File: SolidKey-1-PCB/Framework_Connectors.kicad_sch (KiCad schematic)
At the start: 2 parts, among them J701 Conn_02x25_Counter_Clockwise, J702 Conn_02x25_Counter_Clockwise

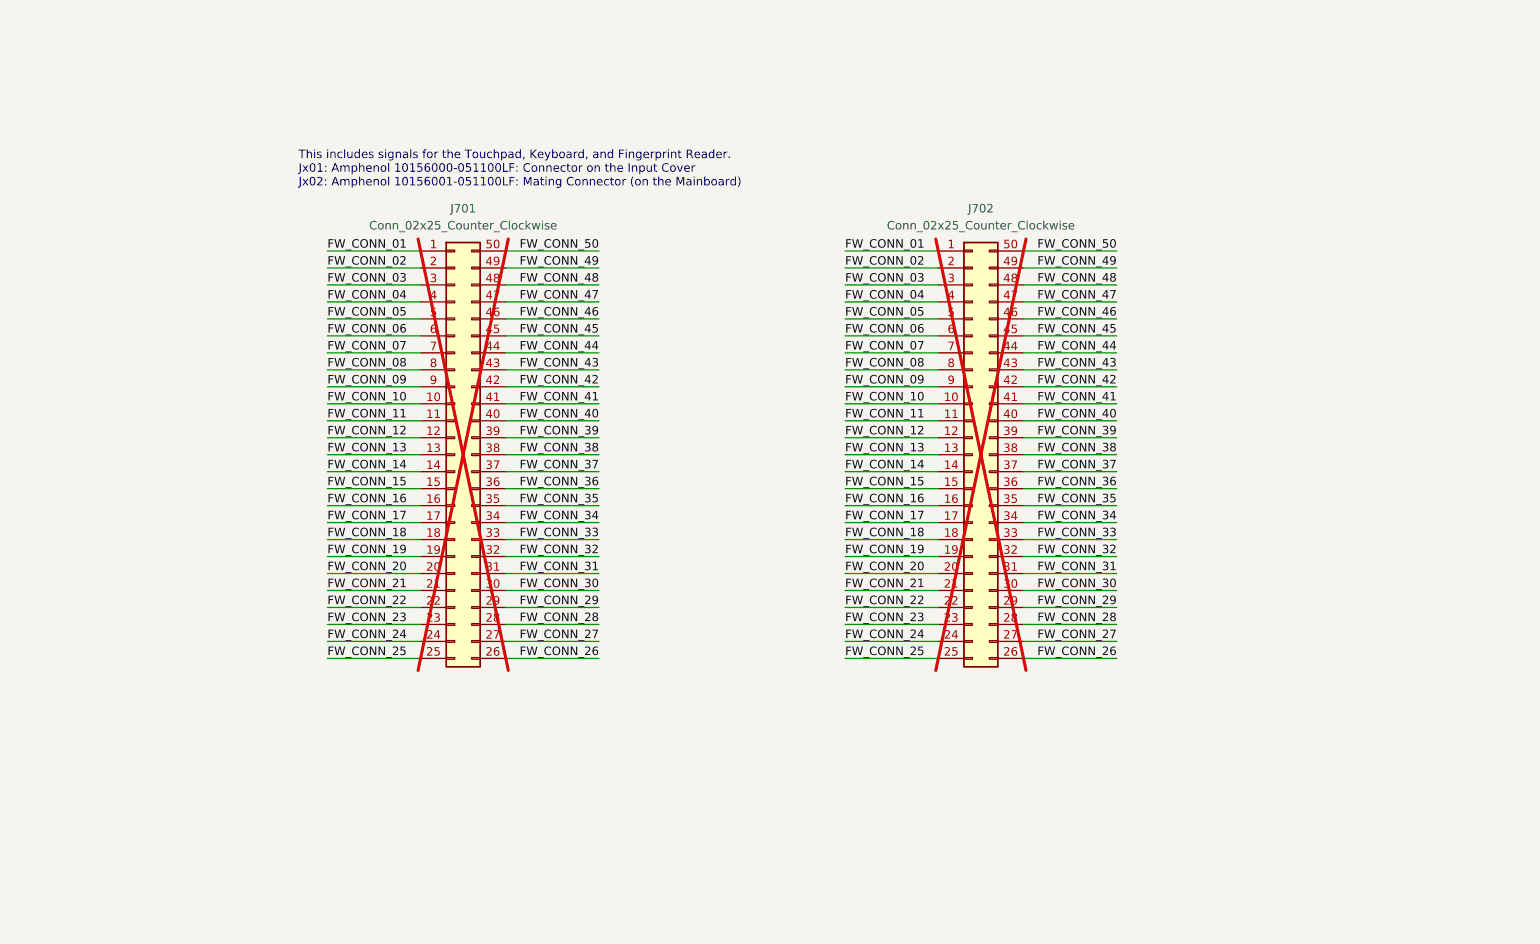
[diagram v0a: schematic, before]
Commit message: Add Framwork connectors and start routing
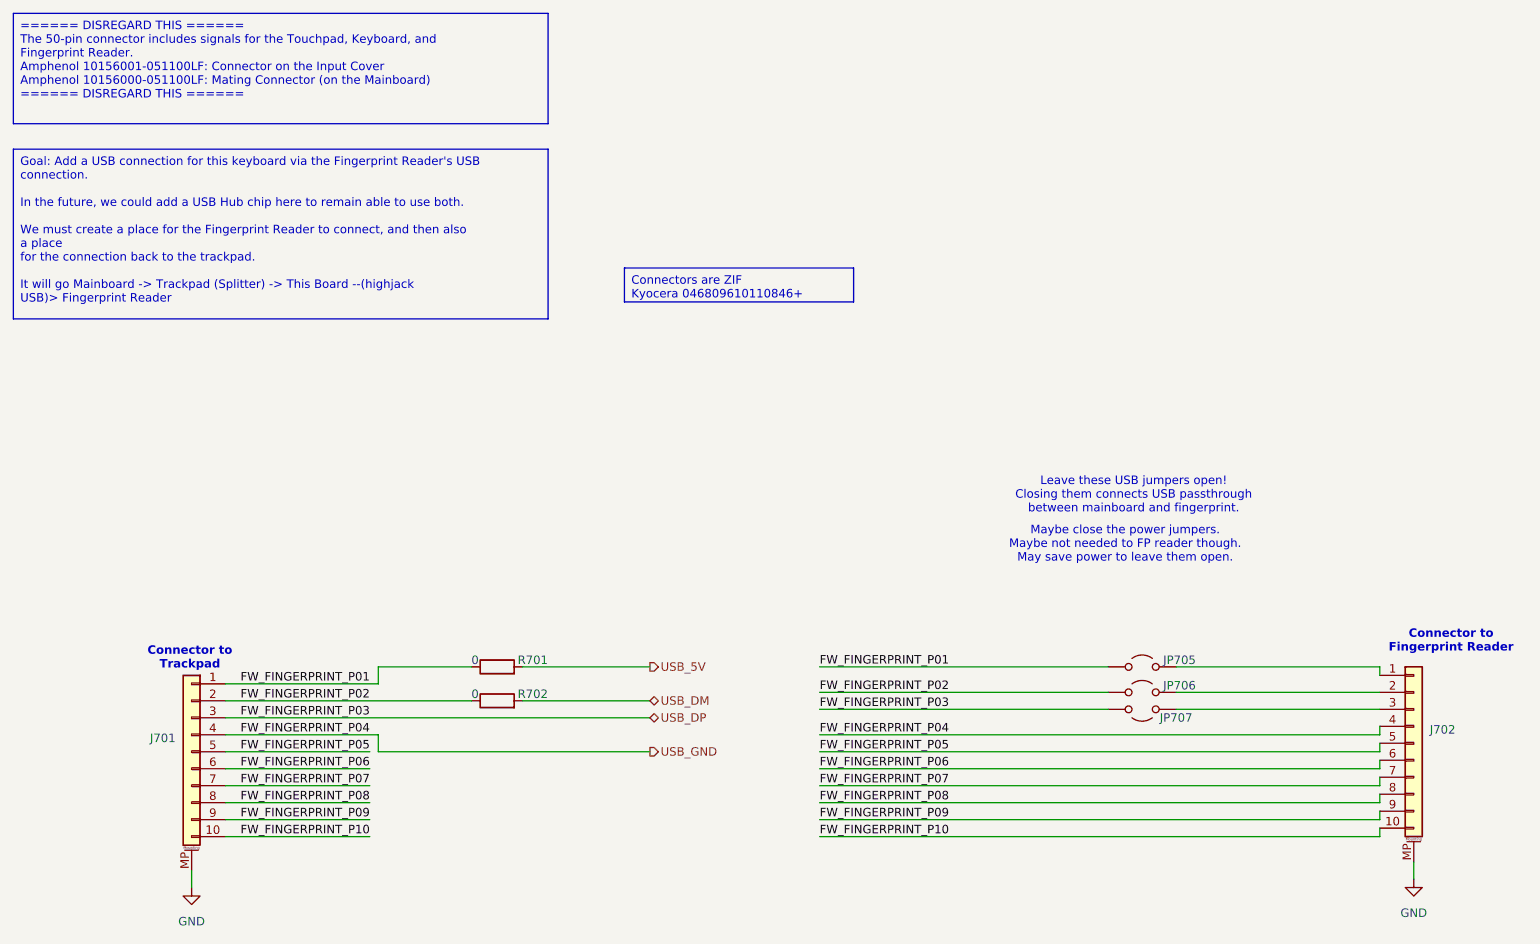
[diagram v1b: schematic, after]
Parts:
- removed J701: Conn_02x25_Counter_Clockwise, Connector_Molex:Molex_SlimStack_52991-0508_2x25_P0.50mm_Vertical, symbol Connector_Generic:Conn_02x25_Counter_Clockwise
- removed J702: Conn_02x25_Counter_Clockwise, symbol Connector_Generic:Conn_02x25_Counter_Clockwise
- added J701, J702: Conn_01x10_MountingPin, SolidKey1_Footprints:046809610110846, symbol Connector_Generic_MountingPin:Conn_01x10_MountingPin
- added JP705, JP706, JP707: Jumper_2_Open, SolidKey1_Footprints:SolderJumper-2_P1.3mm_Open_XSilk_RoundedPad1.0x1.5mm, symbol Jumper:Jumper_2_Open
- added R701, R702: 0, Resistor_SMD:R_0603_1608Metric, symbol Device:R
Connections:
- new net: J702.1 (Pin_1), JP705.1 (A)
- new net: J702.2 (Pin_2), JP706.1 (A)
- new net: J702.3 (Pin_3), JP707.1 (A)
- new net FW_FINGERPRINT_P01: J701.1 (Pin_1), JP705.2 (B), R701.1
- new net FW_FINGERPRINT_P02: J701.2 (Pin_2), JP706.2 (B), R702.1
- new net FW_FINGERPRINT_P05: J701.5 (Pin_5), J702.5 (Pin_5)
- new net FW_FINGERPRINT_P06: J701.6 (Pin_6), J702.6 (Pin_6)
- new net FW_FINGERPRINT_P07: J701.7 (Pin_7), J702.7 (Pin_7)
- new net FW_FINGERPRINT_P08: J701.8 (Pin_8), J702.8 (Pin_8)
- new net FW_FINGERPRINT_P09: J701.9 (Pin_9), J702.9 (Pin_9)
- new net FW_FINGERPRINT_P10: J701.10 (Pin_10), J702.10 (Pin_10)
- new net GND: J701.MP (MountPin), J702.MP (MountPin)
- new net USB_5V: R701.2
- new net USB_DM: R702.2
- new net USB_DP: J701.3 (Pin_3), JP707.2 (B)
- new net USB_GND: J701.4 (Pin_4), J702.4 (Pin_4)
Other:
- note added: "Connector to Fingerprint Reader"
- note added: "Connector to Trackpad"
- note added: "Leave these USB jumpers open! Closing them connects USB passthrough between mainboard and fingerprint."
- note added: "Maybe close the power jumpers. Maybe not needed to FP reader though. May save power to leave them open."
- note removed: "This includes signals for the Touchpad, Keyboard, and Fingerprint Reader. Jx01: Amphenol 10156000-051100LF: Connector on the Input Cover Jx02: Amphenol 10156001-051100LF: Mating Connector (on the Mainboard)"
